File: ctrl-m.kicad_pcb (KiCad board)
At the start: 2 copper layers, 171 x 50.5 mm, 37 parts, among them J1 USB_B, J10 Conn_01x04, J11 Conn_01x05, J12 Conn_01x04, J2 Conn_ARM_JTAG_SWD_10, J3 Conn_01x01, J4 Conn_01x01, J5 Conn_01x01, J6 Conn_01x01, J7 Conn_01x16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

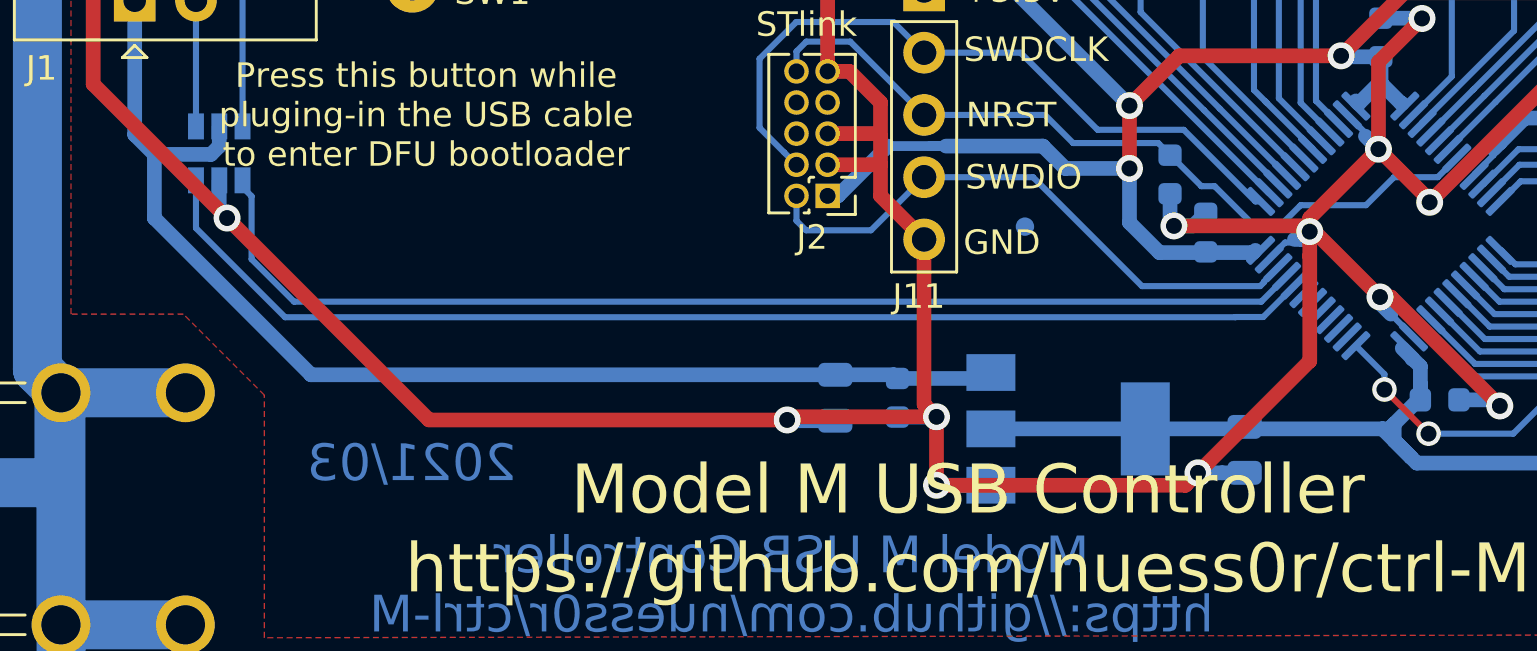
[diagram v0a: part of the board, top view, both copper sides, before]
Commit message: Changed LDO type to one that is stable with ceramic capacitors
LD1117 is unstable with this low output capacitance and in general with
ceramic capacitors.

Also it needs 10 mA minimum load which is not guaranteed when all LEDs are off.

Replaced with a much more recent chip the XC6206P332PR
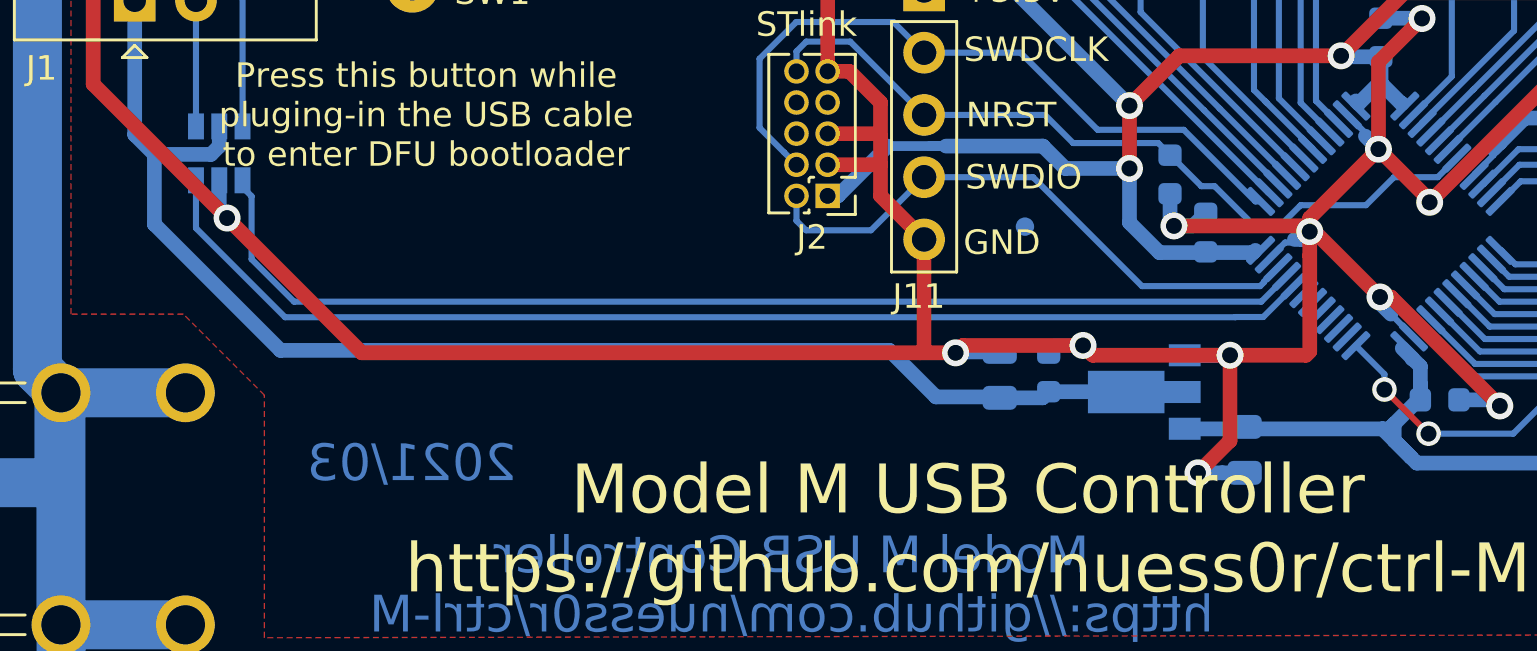
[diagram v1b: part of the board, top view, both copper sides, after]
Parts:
- U2: value LD1117S33TR_SOT223 -> XC6206P332PR; footprint Package_TO_SOT_SMD:SOT-223-3_TabPin2 -> Package_TO_SOT_SMD:SOT-89-3
- moved C1 6.77 mm to (116.4, 100.3), turned to 90 degrees
- moved C2 6.26 mm to (118.4, 100.2), turned to 90 degrees
- moved U2 3.45 mm to (122.3, 101.0), turned to 180 degrees
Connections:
- U2 pad 2: +3V3 -> VBUS
- U2 pad 3: VBUS -> +3V3
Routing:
- net VBUS: track 49.9 -> 58.0 mm
- net +3V3: track 274.8 -> 266.9 mm
- net GND: track 165.5 -> 161.4 mm

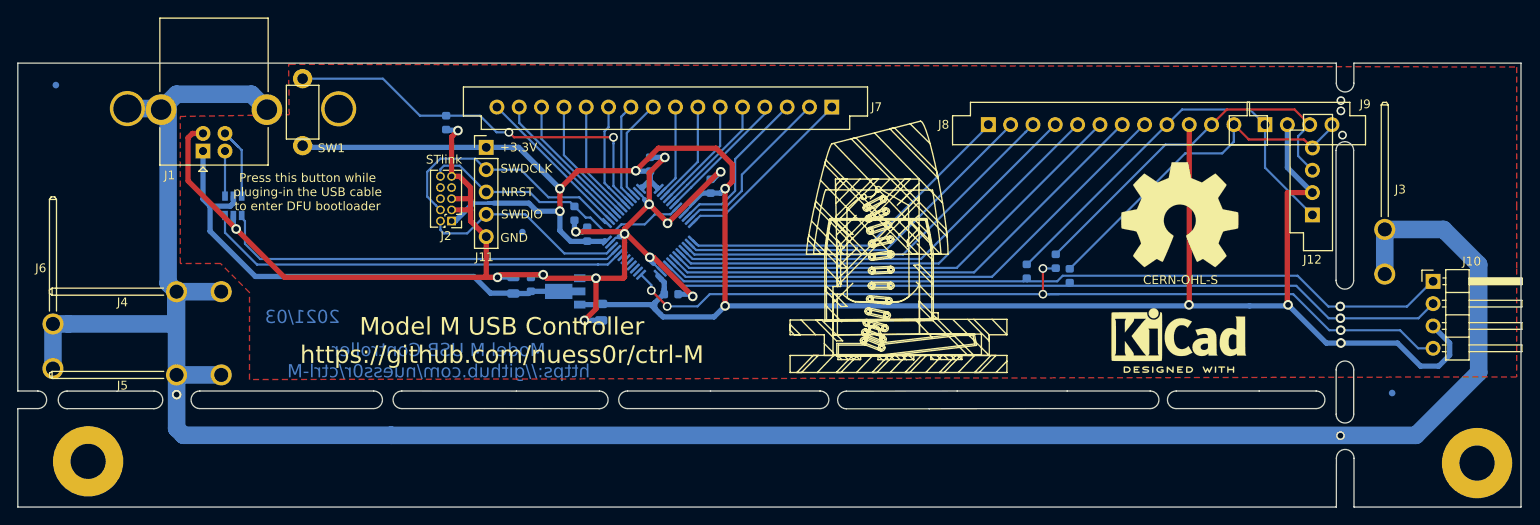
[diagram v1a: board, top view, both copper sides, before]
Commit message: Optimize for production
Applied design rules of prototype manufacturer
Fixed DRC errors
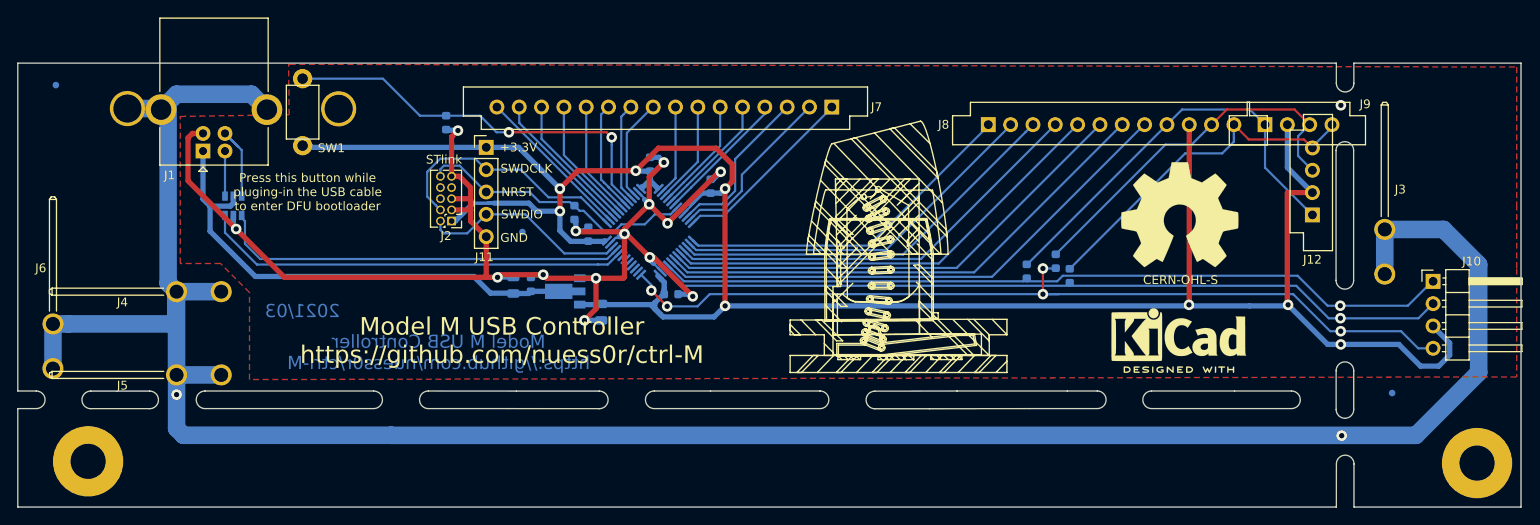
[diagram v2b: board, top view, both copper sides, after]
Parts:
- moved C7 0.12 mm to (124.9, 94.5)
- moved C4 0.09 mm to (123.3, 92.0)
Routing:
- net GND: track 161.4 -> 160.7 mm, vias 17 -> 15
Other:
- outline, holes or cut-outs redrawn
- net class Default: via_dia 1 -> 1.2; via_drill 0.65 -> 0.6
- net class earth: via_dia 1.1 -> 1.2; via_drill 0.65 -> 0.6
- net class power: via_dia 1.1 -> 1.2; via_drill 0.65 -> 0.6
- rule via_min_size: 0.4 -> 0.6

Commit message: Update PCB to wider holes for the plastic pegs and J10 wiring fix
This solves issue #3 and #4
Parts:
- added H5: MountingHole, MountingHole:MountingHole_2.1mm, F.Cu at (87.9, 88.2)
- moved J11 0.48 mm to (113.3, 85.1)
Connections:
- J10 pad 1: /NumLock -> /CapsLock
- J10 pad 2: /ScrollLock -> +3V3
- J10 pad 3: +3V3 -> /ScrollLock
- J10 pad 4: /CapsLock -> /NumLock
- J2 pad 6: Net-(J2-Pad6) -> unconnected-(J2-Pad6)
- J2 pad 7: Net-(J2-Pad7) -> unconnected-(J2-Pad7)
- J2 pad 8: Net-(J2-Pad8) -> unconnected-(J2-Pad8)
- U3 pad 26: Net-(U3-Pad26) -> unconnected-(U3-Pad26)
- U3 pad 27: Net-(U3-Pad27) -> unconnected-(U3-Pad27)
- U3 pad 28: Net-(U3-Pad28) -> unconnected-(U3-Pad28)
- U3 pad 29: Net-(U3-Pad29) -> unconnected-(U3-Pad29)
- U3 pad 30: Net-(U3-Pad30) -> unconnected-(U3-Pad30)
- U3 pad 31: Net-(U3-Pad31) -> unconnected-(U3-Pad31)
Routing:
- net /NumLock: track 91.3 -> 96.3 mm
- net +3V3: track 266.9 -> 269.4 mm
- net Net-(J1-Pad3): track 10.1 -> 7.92 mm
- net /CapsLock: track 101.3 -> 102.8 mm
- net Earth: track 267.6 -> 267.8 mm, vias 2 -> 5
- net (no net): vias 0 -> 15
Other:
- net class Default removed
- net class earth removed
- net class power removed

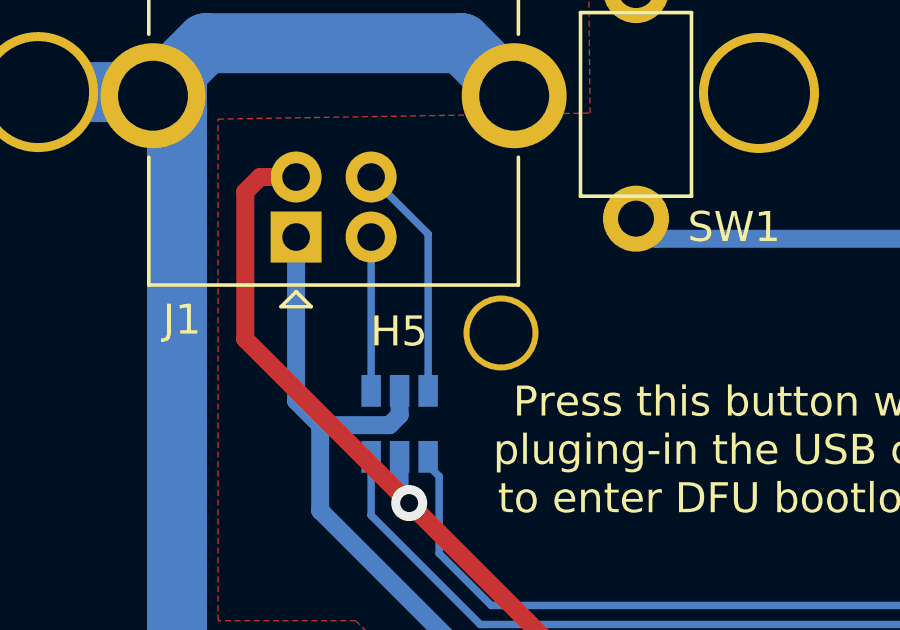
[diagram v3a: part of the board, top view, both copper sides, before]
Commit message: Move button_lever to correct position (change on PCB and 3D model)
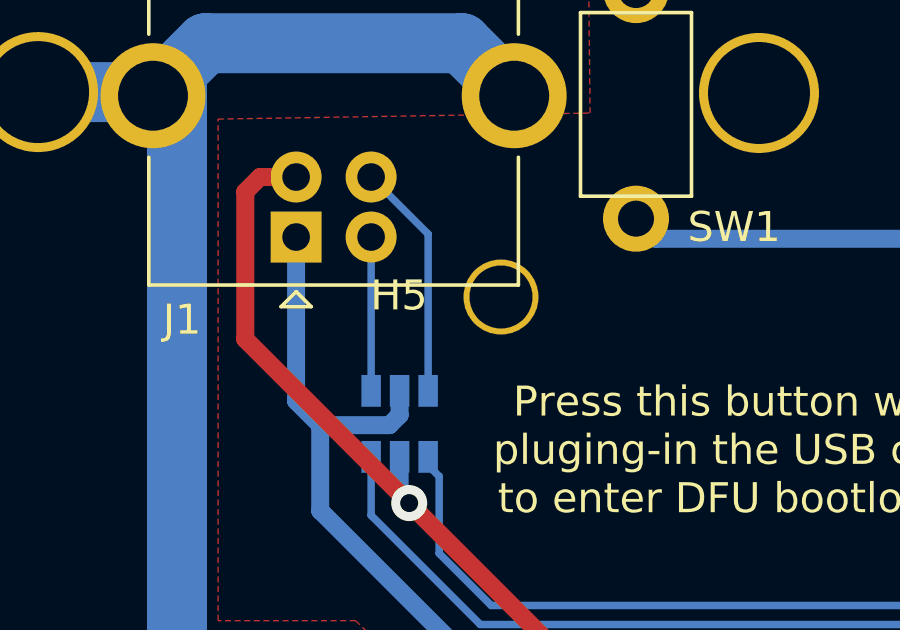
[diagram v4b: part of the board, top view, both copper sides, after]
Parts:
- moved H5 1.20 mm to (87.9, 87.0)
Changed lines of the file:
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@@
   )
   (footprint "MountingHole:MountingHole_2.1mm" locked (layer "F.Cu")
-    (at 87.9 88.199)
+    (at 87.9 87)
     (descr "Mounting Hole 2.1mm, no annular")
     (tags "mounting hole 2.1mm no annular")

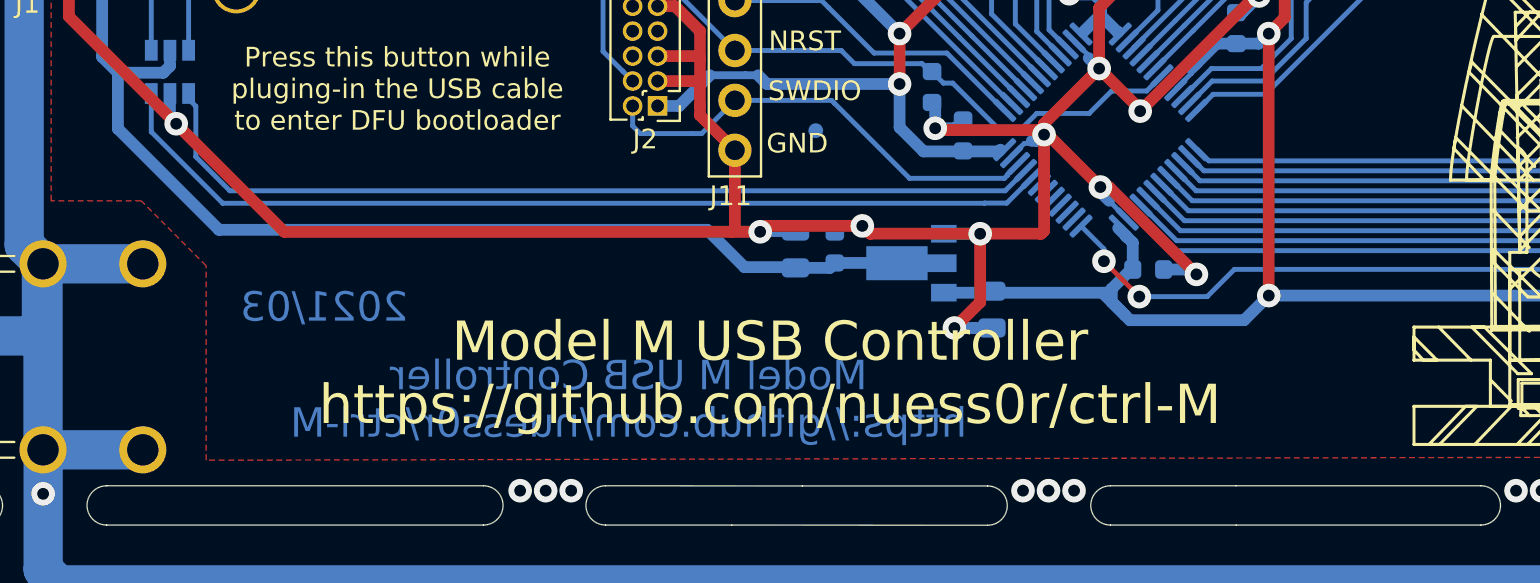
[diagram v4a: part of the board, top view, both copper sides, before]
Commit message: Enhancement: have unused pins ending on a pad #8
Also migrated to KiCAD 9
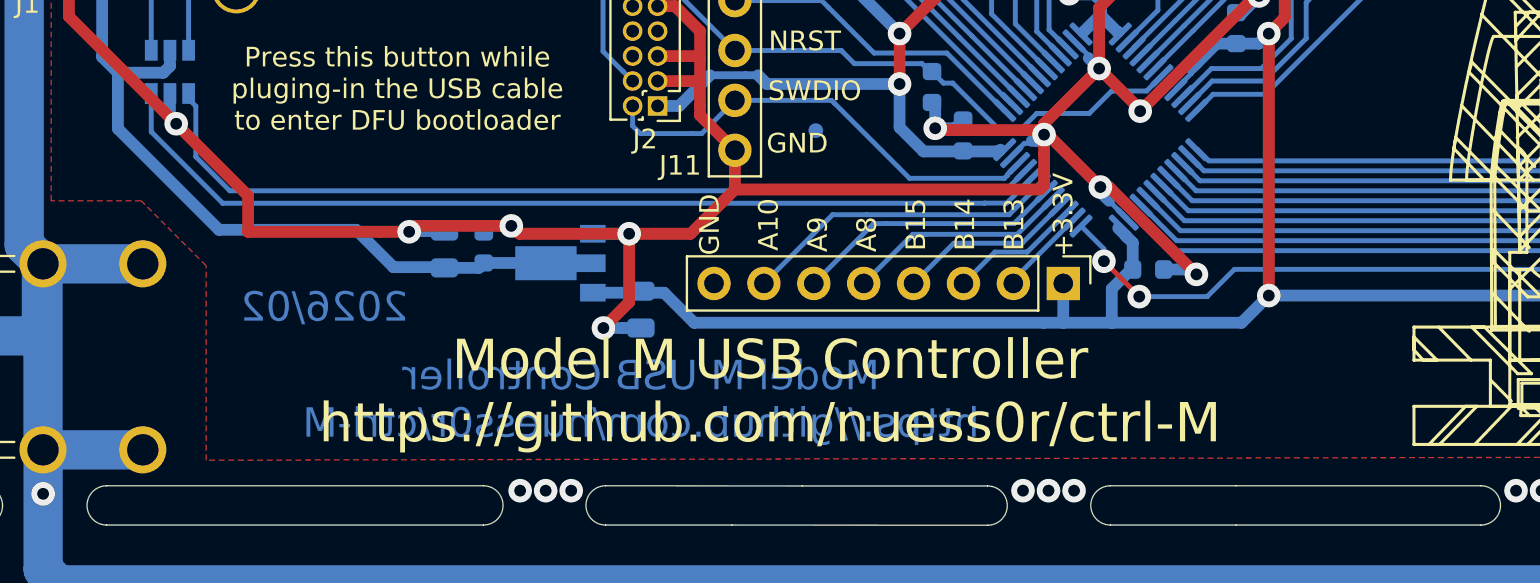
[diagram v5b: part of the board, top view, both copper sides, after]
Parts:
- added J13: Conn_01x08, Connector_PinHeader_2.54mm:PinHeader_1x08_P2.54mm_Vertical, F.Cu at (130.0, 102.0)
- moved C1 17.9 mm to (98.5, 100.3)
- moved C2 17.9 mm to (100.5, 100.2)
- moved C3 17.9 mm to (108.5, 103.3)
- moved U2 17.9 mm to (104.4, 101.0)
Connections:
- H5 pad : GND -> (no net)
- U3 pad 26: unconnected-(U3-Pad26) -> /B13
- U3 pad 27: unconnected-(U3-Pad27) -> /B14
- U3 pad 28: unconnected-(U3-Pad28) -> /B15
- U3 pad 29: unconnected-(U3-Pad29) -> /A8
- U3 pad 30: unconnected-(U3-Pad30) -> /A9
- U3 pad 31: unconnected-(U3-Pad31) -> /A10
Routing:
- net +3V3: track 269.4 -> 288.9 mm
- net VBUS: track 58.0 -> 40.2 mm
- net /A10: track 0.00 -> 16.1 mm
- net /A9: track 0.00 -> 13.8 mm
- net /A8: track 0.00 -> 11.4 mm
- net /B15: track 0.00 -> 9.11 mm
- net /B14: track 0.00 -> 6.78 mm
- net /B13: track 0.00 -> 4.59 mm
- net GND: track 160.7 -> 158.2 mm
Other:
- board text added: "2026/02"
- board text added: "A10"
- board text added: "A8"
- board text added: "A9"
- board text added: "B13"
- board text added: "B14"
- board text added: "B15"
- board text removed: "2021/03"
